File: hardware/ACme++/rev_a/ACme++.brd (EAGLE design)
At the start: 72.6 x 47.1 mm, 92 parts, among them J1 AC-PLUG, J2 TC2030-CTX-NL, J3 WIRE_HOLE-14AWG, J4 WIRE_HOLE-14AWG, J5 WIRE_HOLE-14AWG, K1 S216S01F, Q1 STGD5NB120SZT4, Q2 FDV301N, U1 CC2538, U2 DS2411, U3 FM25LBTDFN-8, U4 ADE7753, U5 TXB0104RGY, U6 SR086SG-G, U7 TDA3664AT, X1 EPSON-FA-128, X2 FC-12M32.7680KA-A3, X3 ECS-35-17-5PX-TR

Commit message: updates to acme++
- no plated earth gnd
- added test points
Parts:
- removed C36, C37: (no value), powercube:2917
- removed J1: AC-PLUG, powercube:AC_MALE_PINS
- added TP1, TP2, TP3, TP4, TP5, TP6, TP7: TEST_POINT_0.040IN, headers:TESTPOINT_0.040IN
- J5: value WIRE_HOLE-14AWG -> AC-PLUG-2; device powercube:WIRE_HOLE-14AWG -> powercube:AC_MALE_PINS_2
- moved J5 22.0 mm to (64.0, 23.5), turned to 180 degrees
- moved J4 3.81 mm to (52.7, 42.9)
- moved R8 2.07 mm to (54.4, 32.4), turned to 270 degrees
- moved C10 1.63 mm to (43.8, 33.4)
- moved R9 1.63 mm to (46.5, 33.4)
- moved C9 1.53 mm to (51.8, 32.4), turned to 90 degrees
- moved J3 1.27 mm to (45.6, 42.9)
- moved R23 1.27 mm to (49.1, 32.4)
- moved L1 1.27 mm to (46.5, 29.0)
- moved C31 0.81 mm to (32.8, 33.5), turned to 0 degrees
- turned C8 to 180 degrees
- turned R14 to 270 degrees
- turned R7 to 0 degrees
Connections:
- removed net EARTH_GND: J1.GND, J5.P$1
- removed net WALL_NEUTRAL_EMI: C10.2, C8.2, C9.2, L2.P$2, R8.1, R9.1
- new net N$14: L2.P$2, R8.1
- net !ADE_CS: now also TP4.TESTPOINT
- net GND: now also C10.2, C8.2, C9.2, R9.1
- net MISO: now also TP2.TESTPOINT
- net MOSI: now also TP1.TESTPOINT
- net SCLK: now also TP3.TESTPOINT
- net V1N: now also TP6.TESTPOINT
- net V1P: now also TP5.TESTPOINT
- net V2P: now also TP7.TESTPOINT
- net WALL_NEUTRAL: now also J5.N1, J5.N10, J5.N11, J5.N12, J5.N2, J5.N3, J5.N4, J5.N5, J5.N6, J5.N7, J5.N8, J5.N9, J5.NEUTRAL; no longer J1.N1, J1.N10, J1.N11, J1.N12, J1.N2, J1.N3, J1.N4, J1.N5, J1.N6, J1.N7, J1.N8, J1.N9, J1.NEUTRAL
- net WALL_PHASE: now also J5.P1, J5.P10, J5.P11, J5.P12, J5.P2, J5.P3, J5.P4, J5.P5, J5.P6, J5.P7, J5.P8, J5.P9, J5.PHASE; no longer J1.P1, J1.P10, J1.P11, J1.P12, J1.P2, J1.P3, J1.P4, J1.P5, J1.P6, J1.P7, J1.P8, J1.P9, J1.PHASE
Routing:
- net WALL_NEUTRAL_EMI: track 31.9 -> 0.00 mm
- net GND: track 30.7 -> 57.6 mm, vias 104 -> 101
- net EARTH_GND: track 20.0 -> 0.00 mm
- net MISO: track 15.0 -> 24.2 mm
- net MOSI: track 19.6 -> 27.8 mm
- net !ADE_CS: track 13.4 -> 19.1 mm, vias 0 -> 1
- net V1P: track 11.2 -> 15.9 mm, vias 0 -> 2
- net V1N: track 28.2 -> 32.6 mm, vias 4 -> 0
- net SCLK: track 22.7 -> 26.1 mm
- net V2P: track 25.3 -> 22.7 mm, vias 2 -> 0
- net N$14: track 0.00 -> 2.43 mm
- net 3V3: track 161.8 -> 159.8 mm, vias 17 -> 16
- net !FRAM_WP: track 11.0 -> 12.4 mm
- net !ADE_IRQ: track 19.2 -> 20.6 mm
- net ADE_AVDD: track 8.34 -> 7.78 mm
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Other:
- board text added: "!ACS"
- board text added: "2014/01/03"
- board text added: "CLK"
- board text added: "MI"
- board text added: "MO"
- board text added: "V1P"
- board text added: "V2P"
- board text added: "VN"
- board text removed: "2014/01/01"

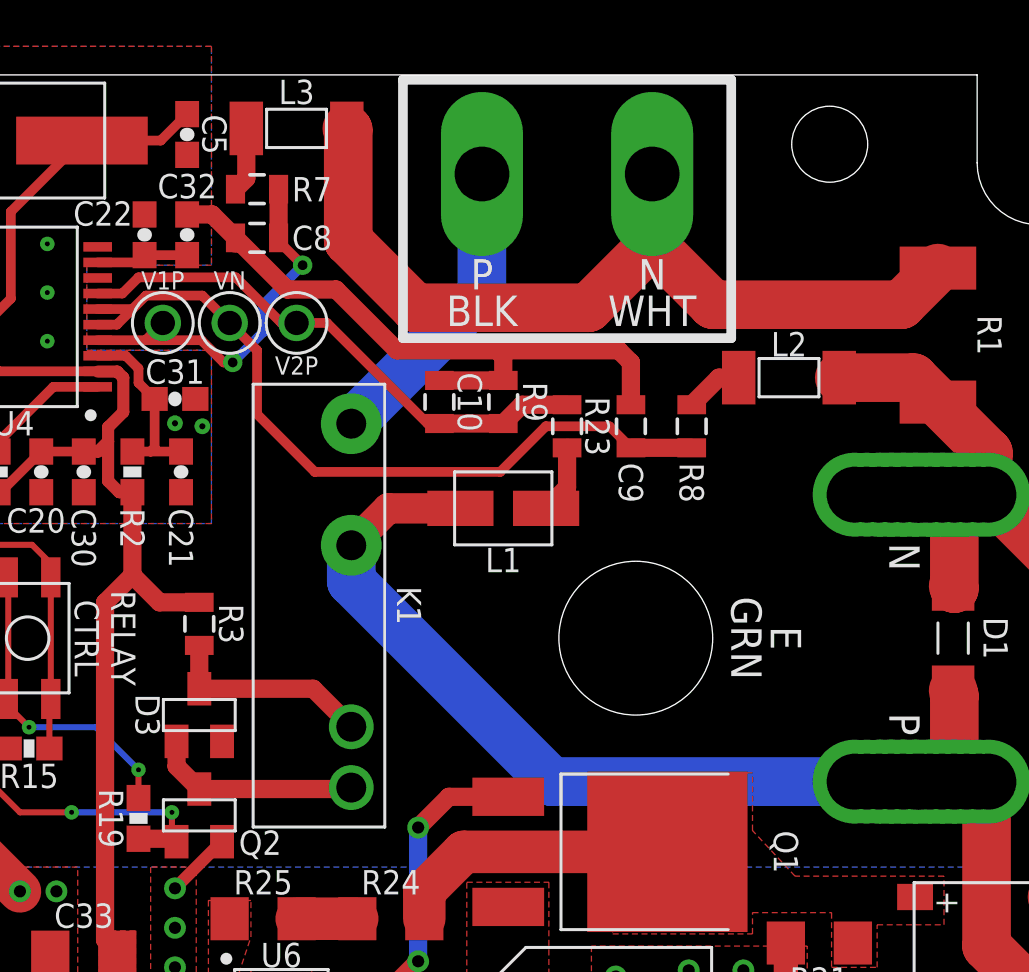
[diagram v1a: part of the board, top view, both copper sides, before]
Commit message: moved relay back
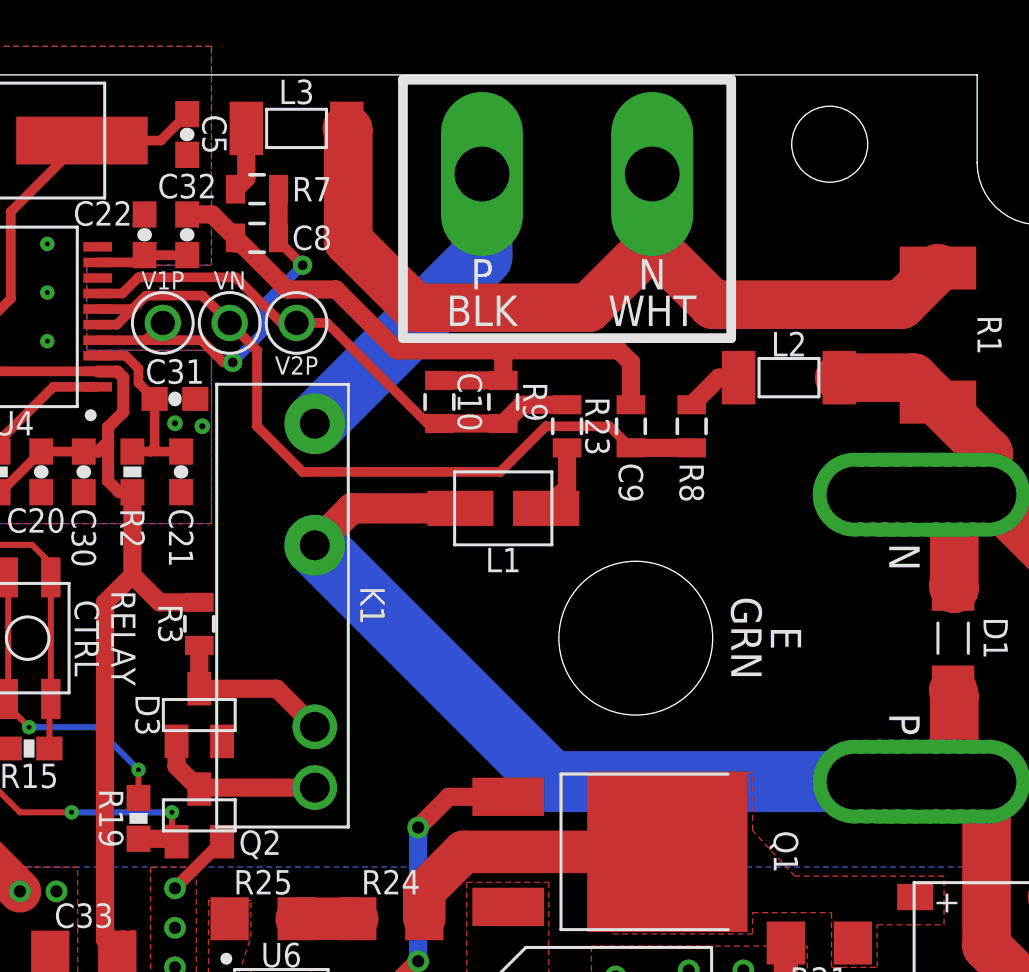
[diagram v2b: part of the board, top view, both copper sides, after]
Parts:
- moved K1 1.52 mm to (38.6, 24.9)
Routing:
- net WALL_PHASE: track 51.1 -> 53.3 mm
- net N$4: track 8.76 -> 7.24 mm
- net N$13: track 8.82 -> 7.29 mm
- net LOAD_PHASE: track 12.7 -> 13.3 mm
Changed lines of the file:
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@@
 <text x="63.881" y="19.939" size="1.27" layer="21" font="vector" ratio="12" rot="SR270" align="top-center">P</text>
 <polygon width="0" layer="30" spacing="0.254" pour="hatch">
-<vertex x="39.624" y="33.02"/>
-<vertex x="40.64" y="32.004"/>
-<vertex x="46.355" y="37.592"/>
+<vertex x="38.1" y="33.02"/>
+<vertex x="39.116" y="32.004"/>
+<vertex x="46.355" y="39.243"/>
 <vertex x="46.355" y="43.18"/>
 <vertex x="44.831" y="43.18"/>
-<vertex x="44.831" y="38.227"/>
+<vertex x="44.831" y="39.751"/>
 </polygon>
 <polygon width="0" layer="30" spacing="0.254" pour="hatch">
-<vertex x="39.37" y="27.559"/>
-<vertex x="40.894" y="27.559"/>
-<vertex x="40.894" y="26.162"/>
+<vertex x="37.973" y="27.051"/>
+<vertex x="38.989" y="28.067"/>
 <vertex x="48.768" y="18.288"/>
 <vertex x="61.214" y="18.288"/>
@@
 </polygon>
 <polygon width="0" layer="32">
-<vertex x="39.37" y="27.178"/>
-<vertex x="40.894" y="27.178"/>
-<vertex x="40.894" y="26.162"/>
+<vertex x="37.973" y="27.051"/>
+<vertex x="38.989" y="28.067"/>
 <vertex x="48.768" y="18.288"/>
 <vertex x="60.579" y="18.288"/>
@@
 <vertex x="44.831" y="43.18"/>
 <vertex x="46.355" y="43.18"/>
-<vertex x="46.355" y="37.592"/>
-<vertex x="40.64" y="32.004"/>
-<vertex x="39.624" y="33.02"/>
-<vertex x="44.831" y="38.227"/>
+<vertex x="46.355" y="39.243"/>
+<vertex x="39.116" y="32.004"/>
+<vertex x="38.1" y="33.02"/>
+<vertex x="44.831" y="39.751"/>
 </polygon>
 <text x="7.366" y="40.767" size="0.762" layer="21" font="vector" ratio="12" align="bottom-center">CLK</text>
@@
 <attribute name="VALUE" x="24.13" y="40.323" size="1.016" layer="27" font="vector" ratio="12" align="bottom-center"/>
 </element>
-<element name="K1" library="powercube" package="RELAY_SX16S0X" value="S216S01F" x="40.132" y="24.892" smashed="yes" rot="R270">
-<attribute name="MOUSER" value="852-S216S01F" x="40.132" y="24.892" size="1.778" layer="27" rot="R270" display="off"/>
-<attribute name="NEWARK" value="14N9591" x="40.132" y="24.892" size="1.778" layer="27" rot="R270" display="off"/>
-<attribute name="DIGIKEY" value="425-2413-5-ND" x="40.132" y="24.892" size="1.778" layer="27" rot="R270" display="off"/>
-<attribute name="NAME" x="42.037" y="24.892" size="1.016" layer="25" font="vector" ratio="12" rot="SR270" align="bottom-center"/>
-<attribute name="VALUE" x="34.417" y="24.892" size="1.016" layer="27" font="vector" ratio="12" rot="R270" align="bottom-center"/>
+<element name="K1" library="powercube" package="RELAY_SX16S0X" value="S216S01F" x="38.608" y="24.892" smashed="yes" rot="R270">
+<attribute name="MOUSER" value="852-S216S01F" x="38.608" y="24.892" size="1.778" layer="27" rot="R270" display="off"/>
+<attribute name="NEWARK" value="14N9591" x="38.608" y="24.892" size="1.778" layer="27" rot="R270" display="off"/>
+<attribute name="DIGIKEY" value="425-2413-5-ND" x="38.608" y="24.892" size="1.778" layer="27" rot="R270" display="off"/>
+<attribute name="NAME" x="40.513" y="24.892" size="1.016" layer="25" font="vector" ratio="12" rot="SR270" align="bottom-center"/>
+<attribute name="VALUE" x="32.893" y="24.892" size="1.016" layer="27" font="vector" ratio="12" rot="R270" align="bottom-center"/>
 </element>
 <element name="D3" library="powercube" package="SOT-23" value="DIODE_MMBD914" x="33.782" y="20.32" smashed="yes">
@@
 <element name="R3" library="SparkFun-Resistors" package="0805" value="330" x="33.782" y="24.13" smashed="yes" rot="R90">
 <attribute name="DIGIKEY" value="RHM330KCT-ND" x="33.782" y="24.13" size="1.778" layer="27" rot="R90" display="off"/>
-<attribute name="NAME" x="34.6075" y="24.13" size="1.016" layer="25" font="vector" ratio="12" rot="SR270" align="bottom-center"/>
+<attribute name="NAME" x="33.0835" y="24.13" size="1.016" layer="25" font="vector" ratio="12" rot="SR270" align="top-center"/>
 <attribute name="VALUE" x="35.179" y="23.114" size="0.4064" layer="27" rot="R90"/>
 </element>
@@
 <wire x1="50.916" y1="32.385" x2="48.26" y2="32.385" width="0.4064" layer="1"/>
 <wire x1="48.26" y1="32.385" x2="46.355" y2="30.48" width="0.4064" layer="1"/>
-<wire x1="46.355" y1="30.48" x2="38.608" y2="30.48" width="0.4064" layer="1"/>
-<wire x1="38.608" y1="30.48" x2="36.195" y2="32.893" width="0.4064" layer="1"/>
+<wire x1="46.355" y1="30.48" x2="38.1" y2="30.48" width="0.4064" layer="1"/>
+<wire x1="38.1" y1="30.48" x2="36.195" y2="32.385" width="0.4064" layer="1"/>
 <wire x1="30.988" y1="37.282" x2="29.535" y2="37.282" width="0.4064" layer="1"/>
 <wire x1="29.535" y1="36.632" x2="30.338" y2="36.632" width="0.4064" layer="1"/>
@@
 <wire x1="33.909" y1="37.846" x2="35.052" y2="36.703" width="0.4064" layer="1"/>
 <wire x1="35.052" y1="36.703" x2="36.195" y2="35.56" width="0.4064" layer="1"/>
-<wire x1="36.195" y1="35.56" x2="36.195" y2="32.893" width="0.4064" layer="1"/>
+<wire x1="36.195" y1="35.56" x2="36.195" y2="32.385" width="0.4064" layer="1"/>
 </signal>
 <signal name="V2P">
@@
 <contactref element="D3" pad="1"/>
 <contactref element="Q2" pad="3"/>
-<wire x1="40.132" y1="17.29" x2="40.071" y2="17.229" width="0.762" layer="1"/>
-<wire x1="40.071" y1="17.229" x2="33.782" y2="17.229" width="0.762" layer="1"/>
 <wire x1="33.782" y1="17.229" x2="32.832" y2="18.179" width="0.762" layer="1"/>
 <wire x1="32.832" y1="18.179" x2="32.832" y2="19.22" width="0.762" layer="1"/>
+<wire x1="33.782" y1="17.229" x2="33.843" y2="17.29" width="0.762" layer="1"/>
+<wire x1="33.843" y1="17.29" x2="38.608" y2="17.29" width="0.762" layer="1"/>
 </signal>
 <signal name="N$13">
@@
 <contactref element="D3" pad="3"/>
 <contactref element="R3" pad="1"/>
-<wire x1="40.132" y1="19.83" x2="38.542" y2="21.42" width="0.762" layer="1"/>
-<wire x1="38.542" y1="21.42" x2="33.782" y2="21.42" width="0.762" layer="1"/>
 <wire x1="33.782" y1="21.42" x2="33.782" y2="23.23" width="0.762" layer="1"/>
+<wire x1="38.608" y1="19.83" x2="37.018" y2="21.42" width="0.762" layer="1"/>
+<wire x1="37.018" y1="21.42" x2="33.782" y2="21.42" width="0.762" layer="1"/>
 </signal>
 <signal name="RELAY_CTRL">
@@
 <wire x1="66.3448" y1="17.5387" x2="66.7512" y2="17.5387" width="0.254" layer="1"/>
 <contactref element="K1" pad="2"/>
-<wire x1="40.132" y1="27.414" x2="41.674" y2="28.956" width="1.27" layer="1"/>
-<wire x1="41.674" y1="28.956" x2="44.6913" y2="28.956" width="1.27" layer="1"/>
+<wire x1="40.15" y1="28.956" x2="44.6913" y2="28.956" width="1.27" layer="1"/>
 <contactref element="J5" pad="PHASE"/>
 <contactref element="J5" pad="P3"/>
@@
 <contactref element="J5" pad="P9"/>
 <contactref element="J5" pad="P11"/>
-<wire x1="61.1632" y1="17.5387" x2="48.5013" y2="17.5387" width="2.032" layer="16"/>
-<wire x1="48.5013" y1="17.5387" x2="40.132" y2="25.908" width="2.032" layer="16"/>
-<wire x1="40.132" y1="25.908" x2="40.132" y2="27.414" width="2.032" layer="16"/>
+<wire x1="38.626" y1="27.414" x2="38.608" y2="27.414" width="2.032" layer="16"/>
+<wire x1="40.15" y1="28.956" x2="38.608" y2="27.414" width="1.27" layer="1"/>
+<wire x1="61.1632" y1="17.5387" x2="48.4833" y2="17.5387" width="2.54" layer="16"/>
+<wire x1="48.4833" y1="17.5387" x2="38.608" y2="27.414" width="2.54" layer="16"/>
 </signal>
 <signal name="LOAD_PHASE">
 <contactref element="J3" pad="P$1"/>
 <contactref element="K1" pad="1"/>
-<wire x1="40.132" y1="32.494" x2="45.593" y2="37.955" width="2.032" layer="16"/>
-<wire x1="45.593" y1="37.955" x2="45.593" y2="42.926" width="2.032" layer="16"/>
+<wire x1="38.608" y1="32.494" x2="45.593" y2="39.479" width="2.54" layer="16"/>
+<wire x1="45.593" y1="39.479" x2="45.593" y2="42.926" width="2.54" layer="16"/>
 </signal>
 <signal name="N$16">

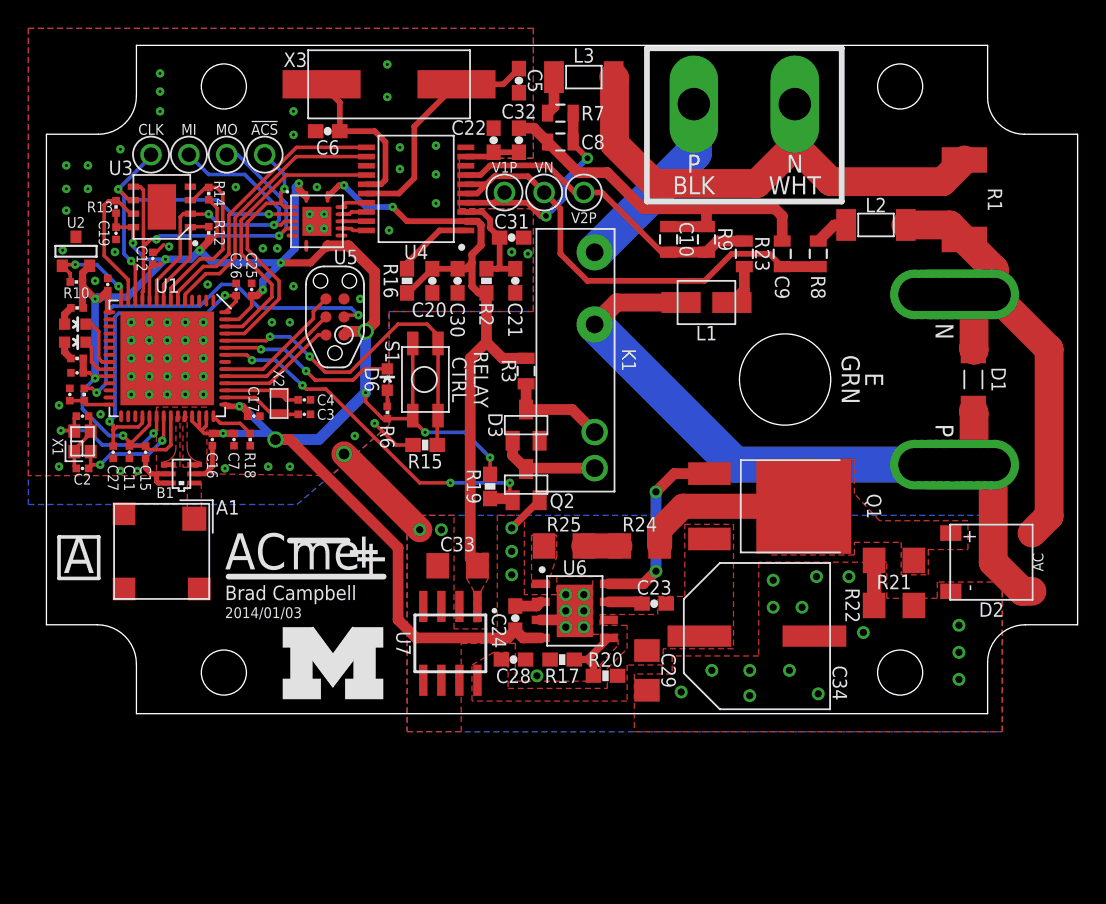
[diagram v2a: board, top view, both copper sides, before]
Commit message: worked on plated cutouts...
I hope sunstone will do something reasonable
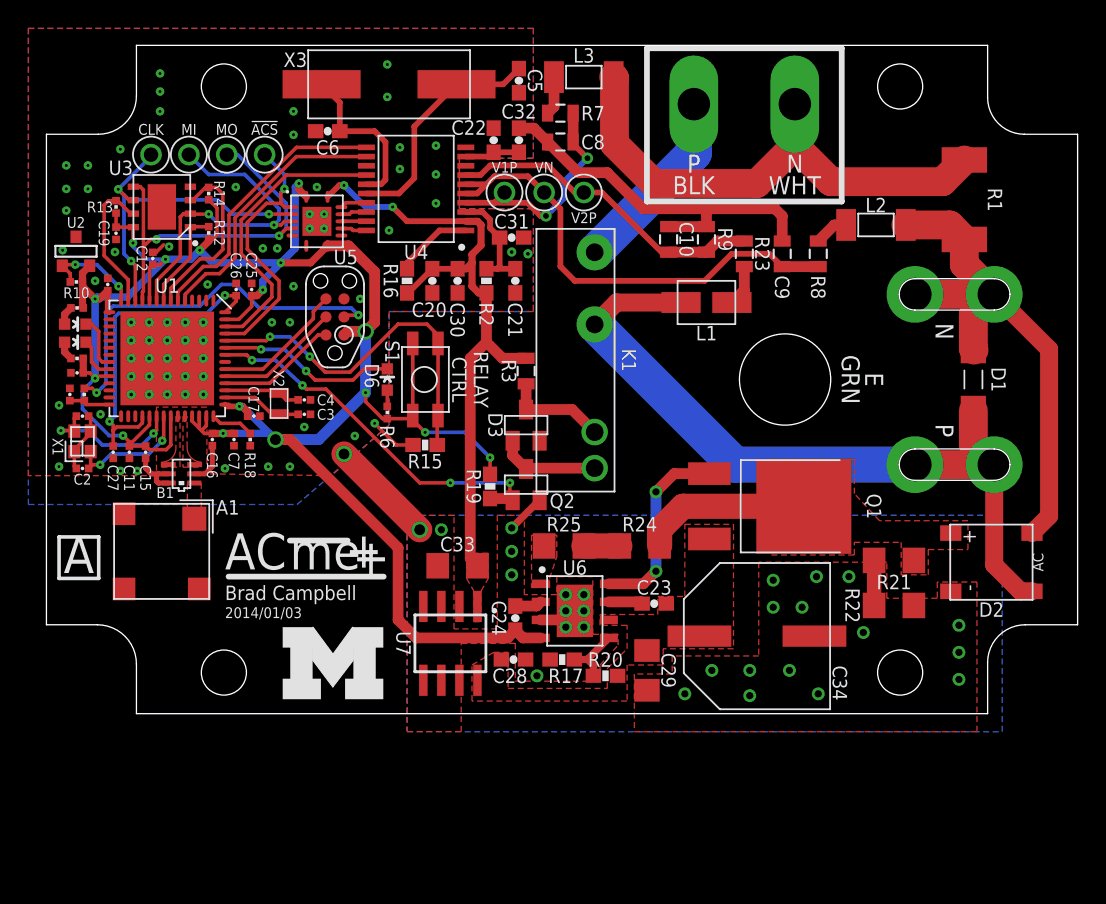
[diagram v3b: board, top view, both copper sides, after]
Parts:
- J5: value AC-PLUG-2 -> (none)
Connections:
- net WALL_NEUTRAL: now also J5.NEUTRAL1, J5.NEUTRAL2; no longer J5.N1, J5.N10, J5.N11, J5.N12, J5.N2, J5.N3, J5.N4, J5.N5, J5.N6, J5.N7, J5.N8, J5.N9, J5.NEUTRAL
- net WALL_PHASE: now also J5.PHASE1, J5.PHASE2; no longer J5.P1, J5.P10, J5.P11, J5.P12, J5.P2, J5.P3, J5.P4, J5.P5, J5.P6, J5.P7, J5.P8, J5.P9, J5.PHASE
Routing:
- net WALL_PHASE: track 53.3 -> 53.9 mm
- net V1N: track 32.8 -> 33.4 mm
- net GND: vias 101 -> 102
